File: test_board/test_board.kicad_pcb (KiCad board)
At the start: 4 copper layers, 68 parts, among them J101 Conn_01x02_Female, J102 Conn_01x04_Female, J103 Conn_01x04_Female, J104 Conn_01x01_Female, K301 KEYSW, K302 KEYSW, K303 KEYSW, K304 KEYSW, K305 KEYSW, K306 KEYSW, K307 KEYSW, K308 KEYSW, K309 KEYSW, K310 KEYSW, K311 KEYSW, K312 KEYSW, K313 KEYSW, K314 KEYSW, K315 KEYSW, K316 KEYSW, U201 WS2811, U202 WS2811, U203 WS2811, U204 WS2811, U205 WS2811, U206 WS2811, U207 WS2811, U208 WS2811, U209 WS2811, U210 WS2811, U211 WS2811, U212 WS2811, U213 WS2811, U214 WS2811, U215 WS2811, U216 WS2811

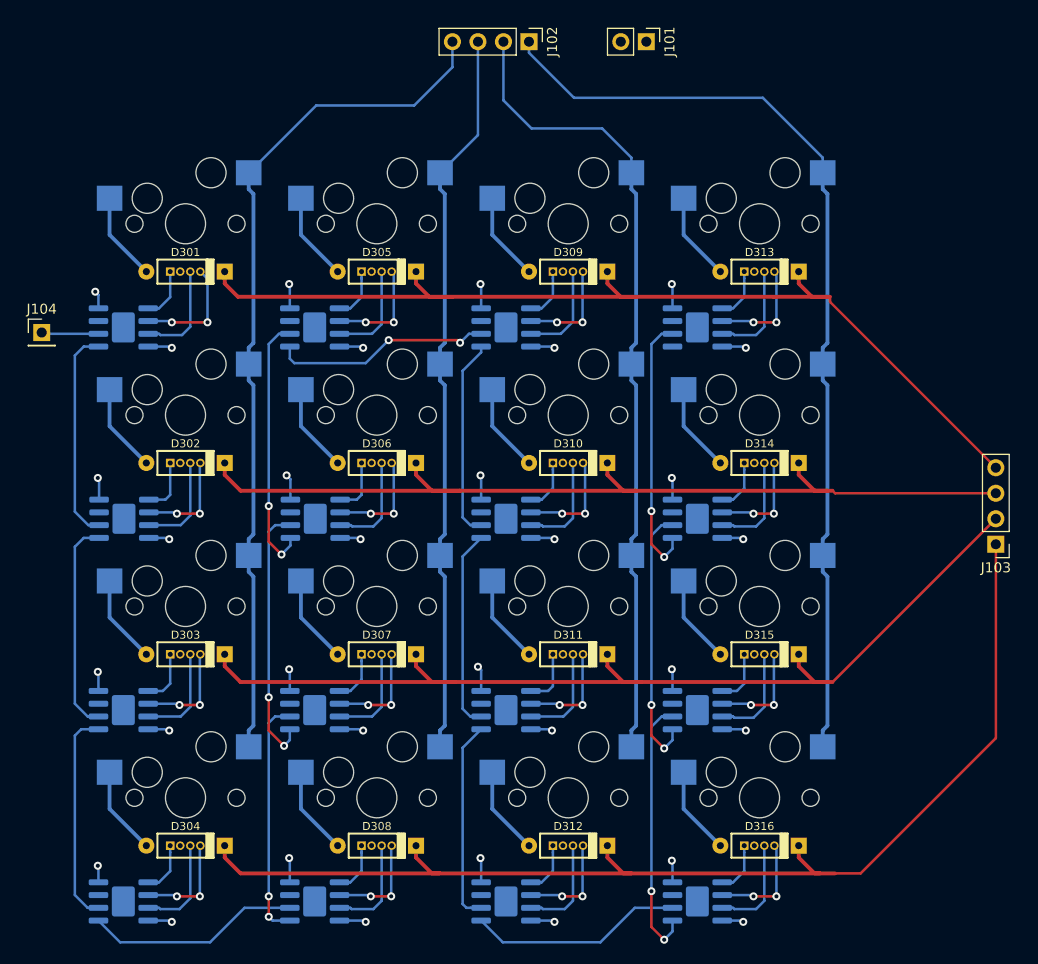
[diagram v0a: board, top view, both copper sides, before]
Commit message: Updated LED footprints
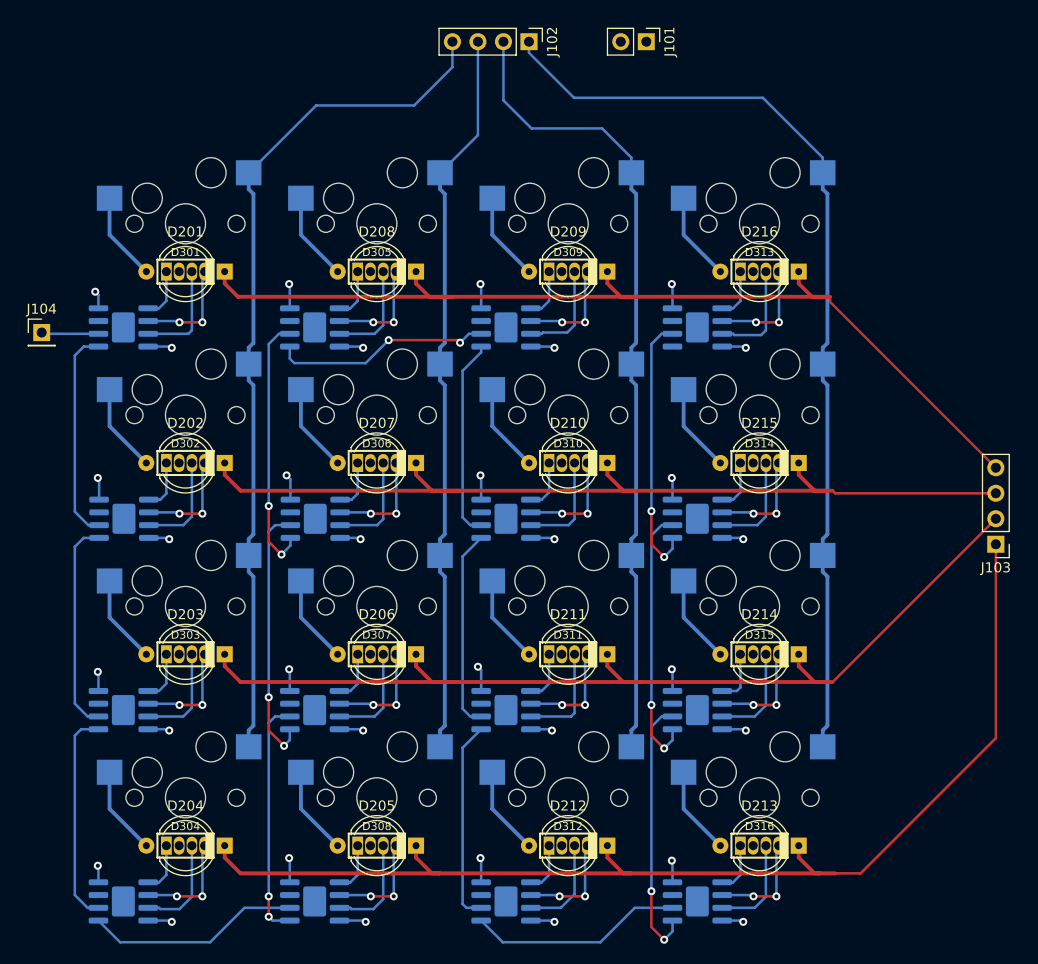
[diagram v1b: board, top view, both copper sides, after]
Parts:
- D201, D202, D203, D204, D205, D206, D207, D208, D209, D210, D211, D212, D213, D214, D215, D216: footprint Connector_PinHeader_1.00mm:PinHeader_1x04_P1.00mm_Horizontal -> LED_THT:LED_D5.0mm-4_RGB; moved to F.Cu
- moved D201 0.38 mm to (39.3, 61.2), turned to 0 degrees
- moved D202 0.38 mm to (39.3, 80.3), turned to 0 degrees
- moved D203 0.38 mm to (39.3, 99.3), turned to 0 degrees
- moved D204 0.38 mm to (39.3, 118.4), turned to 0 degrees
- moved D205 0.38 mm to (58.4, 118.4), turned to 0 degrees
- moved D206 0.38 mm to (58.4, 99.3), turned to 0 degrees
- moved D207 0.38 mm to (58.4, 80.3), turned to 0 degrees
- moved D208 0.38 mm to (58.4, 61.2), turned to 0 degrees
- moved D209 0.38 mm to (77.4, 61.2), turned to 0 degrees
- moved D210 0.38 mm to (77.4, 80.3), turned to 0 degrees
- moved D211 0.38 mm to (77.4, 99.3), turned to 0 degrees
- moved D212 0.38 mm to (77.4, 118.4), turned to 0 degrees
- moved D213 0.38 mm to (96.5, 118.4), turned to 0 degrees
- moved D214 0.38 mm to (96.5, 99.3), turned to 0 degrees
- moved D215 0.38 mm to (96.5, 80.3), turned to 0 degrees
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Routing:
- net Net-(D201-Pad4): track 11.3 -> 10.6 mm
- net Net-(D211-Pad1): track 5.56 -> 5.03 mm
- net Net-(D211-Pad3): track 9.83 -> 10.3 mm
- net Net-(D206-Pad4): track 10.3 -> 10.8 mm

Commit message: update test board schematic to SMD LED
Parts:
- D201, D202, D203, D204, D205, D206, D207, D208, D209, D210, D211, D212, D213, D214, D215, D216: footprint LED_THT:LED_D5.0mm-4_RGB -> keyboard_project:APTF1616SEJ3ZGGVBDC
- moved D201 1.81 mm to (41.1, 61.2)
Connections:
- D201 pad 1: Net-(D201-Pad1) -> GND
- D201 pad 2: GND -> Net-(D201-Pad1)
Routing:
- net Net-(D201-Pad4): track 10.6 -> 0.00 mm, vias 2 -> 0
- net Net-(D201-Pad3): track 10.3 -> 0.00 mm

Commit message: example routing for new LED part
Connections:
- D201 pad 2: Net-(D201-Pad1) -> (no net)
- D201 pad 3: Net-(D201-Pad3) -> (no net)
- D201 pad 4: Net-(D201-Pad4) -> (no net)
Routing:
- net Net-(D201-Pad3): track 0.00 -> 7.85 mm
- net Net-(D201-Pad4): track 0.00 -> 5.84 mm
- net Net-(D201-Pad1): track 5.03 -> 5.79 mm
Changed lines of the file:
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@@
     (thickness 1.6002)
     (drawings 0)
-    (tracks 597)
+    (tracks 604)
     (zones 0)
     (modules 68)
@@
       (effects (font (size 1 1) (thickness 0.15)))
     )
-    (pad 4 smd rect (at 0.875 0.5) (size 0.85 0.5) (layers F.Cu F.Paste F.Mask)
-      (net 12 "Net-(D201-Pad4)"))
-    (pad 3 smd rect (at -0.875 0.5) (size 0.85 0.5) (layers F.Cu F.Paste F.Mask)
-      (net 13 "Net-(D201-Pad3)"))
+    (pad 4 smd rect (at 0.875 0.5) (size 0.85 0.5) (layers F.Cu F.Paste F.Mask))
+    (pad 3 smd rect (at -0.875 0.5) (size 0.85 0.5) (layers F.Cu F.Paste F.Mask))
     (pad 1 smd rect (at 0.875 -0.5) (size 0.85 0.5) (layers F.Cu F.Paste F.Mask)
       (net 1 GND))
-    (pad 2 smd rect (at -0.875 -0.5) (size 0.85 0.5) (layers F.Cu F.Paste F.Mask)
-      (net 14 "Net-(D201-Pad1)"))
+    (pad 2 smd rect (at -0.875 -0.5) (size 0.85 0.5) (layers F.Cu F.Paste F.Mask))
   )
   (module keyboard_project:APTF1616SEJ3ZGGVBDC (layer F.Cu)
@@
   (segment (start 105.41 64.262) (end 121.92 80.772) (width 0.254) (layer F.Cu) (net 11))
   (segment (start 105.41 63.754) (end 105.41 64.262) (width 0.254) (layer F.Cu) (net 11))
+  (segment (start 38.502 66.167) (end 40.132 64.537) (width 0.254) (layer B.Cu) (net 12))
+  (segment (start 37.527 66.167) (end 38.502 66.167) (width 0.254) (layer B.Cu) (net 12))
+  (segment (start 40.132 64.537) (end 40.132 61.976) (width 0.254) (layer B.Cu) (net 12))
+  (segment (start 38.502 67.437) (end 41.91 64.029) (width 0.254) (layer B.Cu) (net 13))
+  (segment (start 37.527 67.437) (end 38.502 67.437) (width 0.254) (layer B.Cu) (net 13))
+  (segment (start 41.91 64.029) (end 41.91 61.976) (width 0.254) (layer B.Cu) (net 13))
   (segment (start 39.33825 62.39975) (end 39.33825 61.24575) (width 0.254) (layer B.Cu) (net 14))
   (segment (start 39.33825 64.16075) (end 39.33825 62.39975) (width 0.254) (layer B.Cu) (net 14))
   (segment (start 38.602 64.897) (end 39.33825 64.16075) (width 0.254) (layer B.Cu) (net 14))
   (segment (start 37.527 64.897) (end 38.602 64.897) (width 0.254) (layer B.Cu) (net 14))
+  (segment (start 39.33825 61.24575) (end 39.878 60.706) (width 0.254) (layer B.Cu) (net 14))
   (via (at 40.64 85.344) (size 0.8) (drill 0.4) (layers F.Cu B.Cu) (net 15))
   (segment (start 37.589 85.217) (end 40.513 85.217) (width 0.254) (layer B.Cu) (net 15))

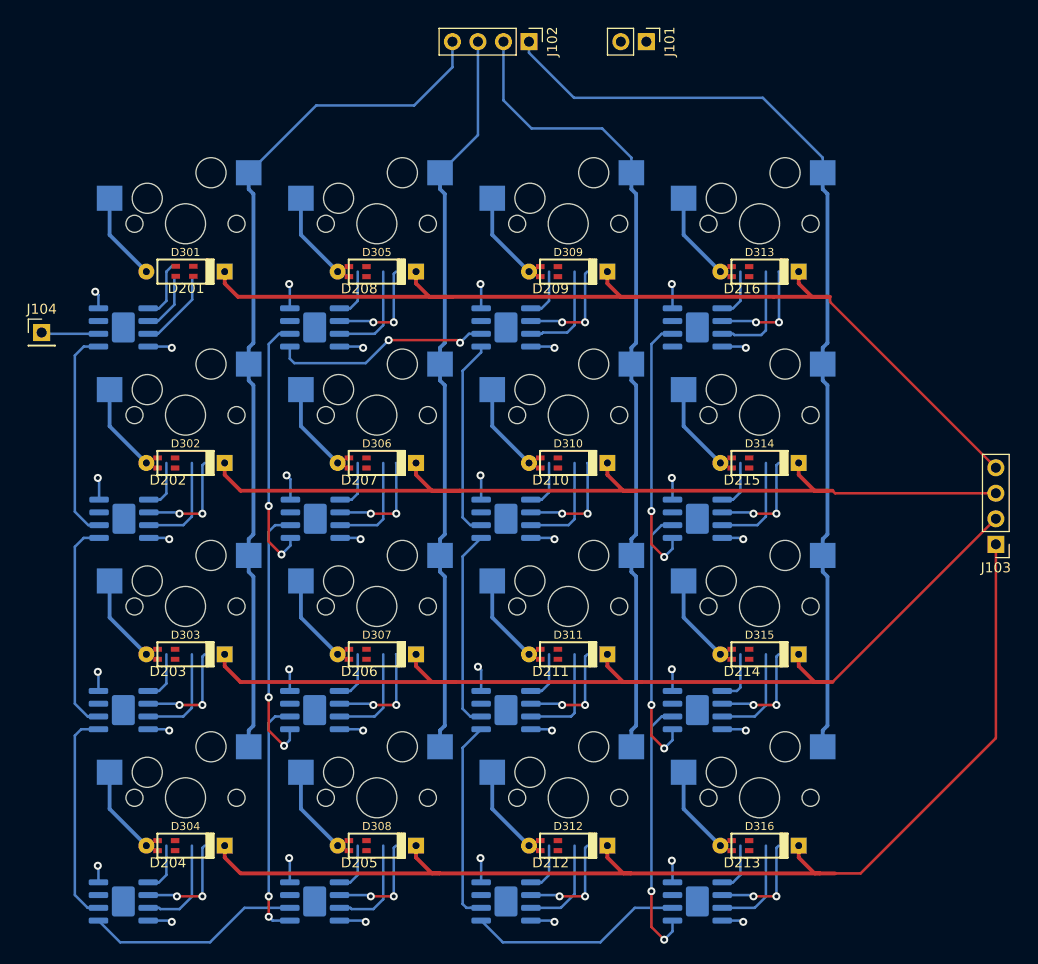
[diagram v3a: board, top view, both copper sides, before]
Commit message: update schematic to CRGB LEDs and move footprints on pcb
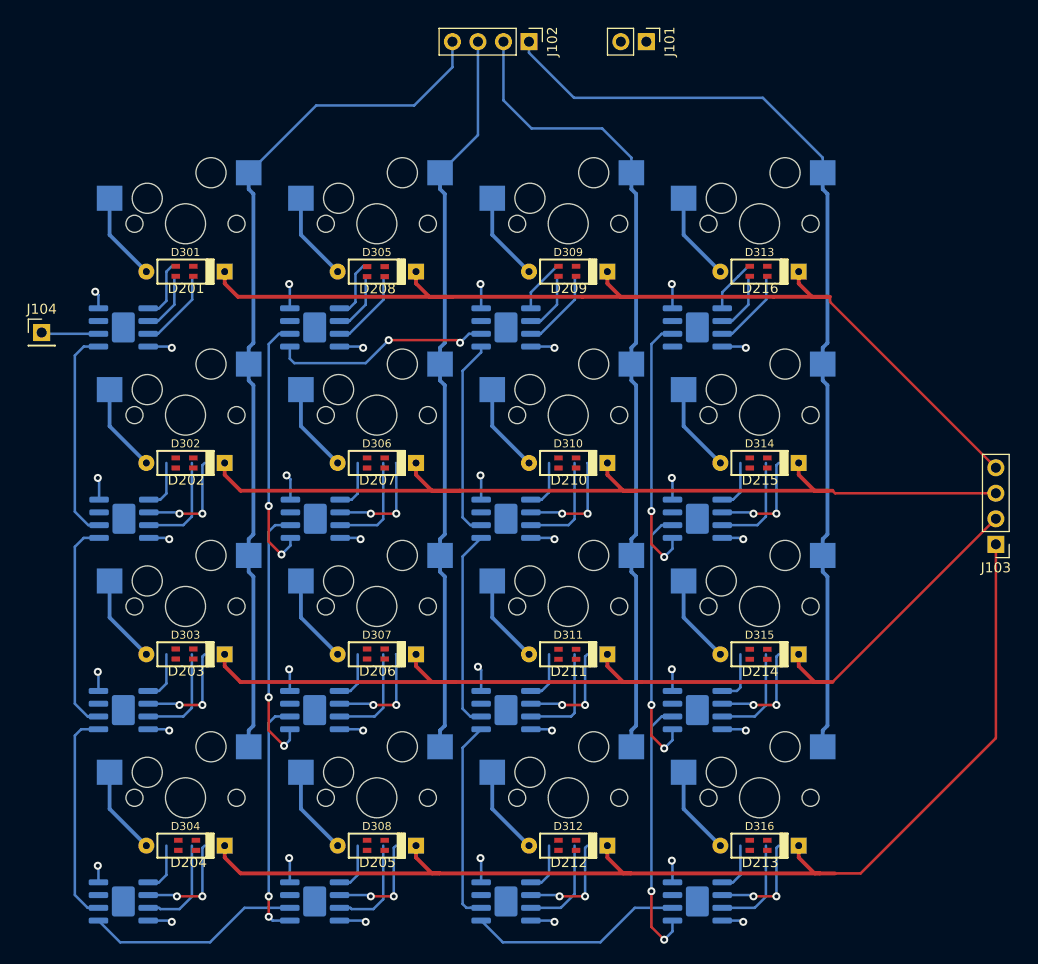
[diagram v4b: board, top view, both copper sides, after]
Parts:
- D201, D202, D203, D204, D205, D206, D207, D208, D209, D210, D211, D212, D213, D214, D215, D216: value LED_RCBG -> LED_CRBG
- moved D204 2.06 mm to (41.4, 118.4)
- moved D209 1.81 mm to (79.2, 61.2)
- moved D212 1.81 mm to (79.2, 118.4)
- moved D213 1.81 mm to (98.3, 118.4)
- moved D216 1.81 mm to (98.3, 61.2)
- moved D203 1.81 mm to (41.1, 99.3)
- moved D205 1.81 mm to (60.2, 118.4)
- moved D206 1.81 mm to (60.2, 99.3)
- moved D210 1.81 mm to (79.2, 80.3)
- moved D211 1.81 mm to (79.2, 99.3)
- moved D214 1.81 mm to (98.3, 99.3)
- moved D215 1.81 mm to (98.3, 80.3)
- moved D202 1.81 mm to (41.1, 80.3)
- moved D207 1.81 mm to (60.2, 80.3)
- moved D208 1.81 mm to (60.2, 61.2)
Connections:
- D201 pad 2: (no net) -> Net-(D201-Pad2)
- D201 pad 3: (no net) -> Net-(D201-Pad3)
- D201 pad 4: (no net) -> Net-(D201-Pad4)
- D202 pad 1: Net-(D202-Pad1) -> GND
- D202 pad 2: GND -> Net-(D202-Pad2)
- D203 pad 1: Net-(D203-Pad1) -> GND
- D203 pad 2: GND -> Net-(D203-Pad2)
- D204 pad 1: Net-(D204-Pad1) -> GND
- D204 pad 2: GND -> Net-(D204-Pad2)
- D205 pad 1: Net-(D205-Pad1) -> GND
- D205 pad 2: GND -> Net-(D205-Pad2)
- D206 pad 1: Net-(D206-Pad1) -> GND
- D206 pad 2: GND -> Net-(D206-Pad2)
- D207 pad 1: Net-(D207-Pad1) -> GND
- D207 pad 2: GND -> Net-(D207-Pad2)
- D208 pad 1: Net-(D208-Pad1) -> GND
- D208 pad 2: GND -> Net-(D208-Pad2)
- D209 pad 1: Net-(D209-Pad1) -> GND
- D209 pad 2: GND -> Net-(D209-Pad2)
- D210 pad 1: Net-(D210-Pad1) -> GND
- D210 pad 2: GND -> Net-(D210-Pad2)
- D211 pad 1: Net-(D211-Pad1) -> GND
- D211 pad 2: GND -> Net-(D211-Pad2)
- D212 pad 1: Net-(D212-Pad1) -> GND
- D212 pad 2: GND -> Net-(D212-Pad2)
- D213 pad 1: Net-(D213-Pad1) -> GND
- D213 pad 2: GND -> Net-(D213-Pad2)
- D214 pad 1: Net-(D214-Pad1) -> GND
- D214 pad 2: GND -> Net-(D214-Pad2)
- D215 pad 1: Net-(D215-Pad1) -> GND
- D215 pad 2: GND -> Net-(D215-Pad2)
- D216 pad 1: Net-(D216-Pad1) -> GND
- D216 pad 2: GND -> Net-(D216-Pad2)
- U201 pad 1: Net-(D201-Pad1) -> Net-(D201-Pad2)
- U201 pad 2: Net-(D201-Pad4) -> Net-(D201-Pad3)
- U201 pad 3: Net-(D201-Pad3) -> Net-(D201-Pad4)
- U202 pad 1: Net-(D202-Pad1) -> Net-(D202-Pad2)
- U202 pad 2: Net-(D202-Pad4) -> Net-(D202-Pad3)
- U202 pad 3: Net-(D202-Pad3) -> Net-(D202-Pad4)
- U203 pad 1: Net-(D203-Pad1) -> Net-(D203-Pad2)
- U203 pad 2: Net-(D203-Pad4) -> Net-(D203-Pad3)
- U203 pad 3: Net-(D203-Pad3) -> Net-(D203-Pad4)
- U204 pad 1: Net-(D204-Pad1) -> Net-(D204-Pad2)
- U204 pad 2: Net-(D204-Pad4) -> Net-(D204-Pad3)
- U204 pad 3: Net-(D204-Pad3) -> Net-(D204-Pad4)
- U205 pad 1: Net-(D205-Pad1) -> Net-(D205-Pad2)
- U205 pad 2: Net-(D205-Pad4) -> Net-(D205-Pad3)
- U205 pad 3: Net-(D205-Pad3) -> Net-(D205-Pad4)
- U206 pad 1: Net-(D206-Pad1) -> Net-(D206-Pad2)
- U206 pad 2: Net-(D206-Pad4) -> Net-(D206-Pad3)
- U206 pad 3: Net-(D206-Pad3) -> Net-(D206-Pad4)
- U207 pad 1: Net-(D207-Pad1) -> Net-(D207-Pad2)
- U207 pad 2: Net-(D207-Pad4) -> Net-(D207-Pad3)
- U207 pad 3: Net-(D207-Pad3) -> Net-(D207-Pad4)
- U208 pad 1: Net-(D208-Pad1) -> Net-(D208-Pad2)
- U208 pad 2: Net-(D208-Pad4) -> Net-(D208-Pad3)
- U208 pad 3: Net-(D208-Pad3) -> Net-(D208-Pad4)
- U209 pad 1: Net-(D209-Pad1) -> Net-(D209-Pad2)
- U209 pad 2: Net-(D209-Pad4) -> Net-(D209-Pad3)
- U209 pad 3: Net-(D209-Pad3) -> Net-(D209-Pad4)
- U210 pad 1: Net-(D210-Pad1) -> Net-(D210-Pad2)
- U210 pad 2: Net-(D210-Pad4) -> Net-(D210-Pad3)
- U210 pad 3: Net-(D210-Pad3) -> Net-(D210-Pad4)
- U211 pad 1: Net-(D211-Pad1) -> Net-(D211-Pad2)
- U211 pad 2: Net-(D211-Pad4) -> Net-(D211-Pad3)
- U211 pad 3: Net-(D211-Pad3) -> Net-(D211-Pad4)
- U212 pad 1: Net-(D212-Pad1) -> Net-(D212-Pad2)
- U212 pad 2: Net-(D212-Pad4) -> Net-(D212-Pad3)
- U212 pad 3: Net-(D212-Pad3) -> Net-(D212-Pad4)
- U213 pad 1: Net-(D213-Pad1) -> Net-(D213-Pad2)
- U213 pad 2: Net-(D213-Pad4) -> Net-(D213-Pad3)
- U213 pad 3: Net-(D213-Pad3) -> Net-(D213-Pad4)
- U214 pad 1: Net-(D214-Pad1) -> Net-(D214-Pad2)
- U214 pad 2: Net-(D214-Pad4) -> Net-(D214-Pad3)
- U214 pad 3: Net-(D214-Pad3) -> Net-(D214-Pad4)
- U215 pad 1: Net-(D215-Pad1) -> Net-(D215-Pad2)
- U215 pad 2: Net-(D215-Pad4) -> Net-(D215-Pad3)
- U215 pad 3: Net-(D215-Pad3) -> Net-(D215-Pad4)
- U216 pad 1: Net-(D216-Pad1) -> Net-(D216-Pad2)
- U216 pad 2: Net-(D216-Pad4) -> Net-(D216-Pad3)
- U216 pad 3: Net-(D216-Pad3) -> Net-(D216-Pad4)
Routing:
- net Net-(D208-Pad2): track 0.00 -> 6.24 mm
- net Net-(D201-Pad2): track 0.00 -> 5.79 mm
- net Net-(D201-Pad1): track 5.79 -> 0.00 mm
- net Net-(D209-Pad2): track 0.00 -> 5.27 mm
- net Net-(D216-Pad2): track 0.00 -> 5.27 mm
- net Net-(D214-Pad2): track 0.00 -> 5.26 mm
- net Net-(D214-Pad1): track 5.26 -> 0.00 mm
- net Net-(D202-Pad2): track 0.00 -> 5.05 mm
- net Net-(D202-Pad1): track 5.05 -> 0.00 mm
- net Net-(D207-Pad2): track 0.00 -> 5.05 mm
- net Net-(D207-Pad1): track 5.05 -> 0.00 mm
- net Net-(D211-Pad2): track 0.00 -> 5.03 mm
- net Net-(D211-Pad1): track 5.03 -> 0.00 mm
- net Net-(D210-Pad2): track 0.00 -> 5.03 mm
- net Net-(D210-Pad1): track 5.03 -> 0.00 mm
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
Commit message: example on pcb of how diodes might go
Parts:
- D201: moved to B.Cu
- D301, D302, D303, D304, D305, D306, D307, D308, D309, D310, D311, D312, D313, D314, D315, D316: footprint keyboard_parts:D_axial -> Diode_SMD:D_SOD-523
- moved D301 1.82 mm to (41.1, 59.4)
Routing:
- net /Row0: track 100.4 -> 104.4 mm
- net Net-(D301-Pad2): track 8.82 -> 10.1 mm, vias 0 -> 1
